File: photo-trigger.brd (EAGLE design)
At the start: 93.4 x 70.3 mm, 49 parts, among them Q1 PN2907, Q2 PN2907, Q3 20MHz, U1 ATMEGA324PA-PU

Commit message: correct device name to match library
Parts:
- VR1, VR2: value RECOMREE-0505S -> RECOM-REE-0505S
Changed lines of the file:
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@@
 <attribute name="VALUE" x="52.07" y="9.525" size="1.27" layer="27"/>
 </element>
-<element name="VR2" library="djm" package="RECOM-REE" value="RECOMREE-0505S" x="39.37" y="59.69"/>
+<element name="VR2" library="djm" package="RECOM-REE" value="RECOM-REE-0505S" x="39.37" y="59.69"/>
 <element name="C3" library="rcl" package="C050-035X075" value="0.1uF" x="49.53" y="63.5" smashed="yes" rot="R180">
 <attribute name="NAME" x="48.006" y="67.056" size="1.27" layer="25" ratio="10" rot="R180"/>
@@
 <attribute name="VALUE" x="6.604" y="20.701" size="1.27" layer="27" ratio="10"/>
 </element>
-<element name="VR1" library="djm" package="RECOM-REE" value="RECOMREE-0505S" x="12.7" y="16.51" smashed="yes" rot="R180">
+<element name="VR1" library="djm" package="RECOM-REE" value="RECOM-REE-0505S" x="12.7" y="16.51" smashed="yes" rot="R180">
 <attribute name="NAME" x="21.59" y="23.495" size="1.27" layer="25" rot="R180"/>
 <attribute name="VALUE" x="22.225" y="14.605" size="1.27" layer="27" rot="R180"/>

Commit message: revised after building v1.0 boards; lots of fixes
ripped out power status indicator circuit - it didn't work.
replaced with a simple power LED.

fixed footprint problem for Recom REE isolated VRMs

rewired LCD socket to be easier to handle at the LCD end

fixed MCU AREF and AGND

expanded prototype area; embiggened pads to make them easier to
solder
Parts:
- removed D1: 6.2V, diode:DO35Z10
- removed Q1, Q2: PN2907, djm:TO92-EBC
- removed R4: 100K, rcl:0207/10
- removed R5: 470, rcl:0207/10
- added +5VI: +5VI, wirepad:1,6/0,9
- added +5VO: +5VO, wirepad:1,6/0,9
- added C8: 0.1uF, rcl:C050-035X075
- added C9: 10uF, rcl:C050-035X075
- added GNDI: GNDI, wirepad:1,6/0,9
- added GNDO: GNDO, wirepad:1,6/0,9
- added GNDP2: GND, wirepad:1,6/0,9
- added VCCP2: VCC, wirepad:1,6/0,9
- LCD: value LCD -> (none)
- R1: value 100K -> 100
- VR1, VR2: value RECOM-REE-0505S -> REE-0505S
- VR3: value RECOM-R-785.0-0.5 -> R-785.0-0.5
- moved R2 75.6 mm to (85.1, 30.5), turned to 90 degrees
- moved C3 40.8 mm to (8.89, 59.7)
- moved C2 31.8 mm to (15.2, 22.9)
- moved VR3 31.8 mm to (8.89, 25.4)
- moved C4 31.7 mm to (15.2, 27.9)
- moved VR2 29.0 mm to (11.4, 52.1), turned to 180 degrees
- moved VR1 26.7 mm to (11.4, 43.2)
- moved R3 19.7 mm to (10.2, 16.5)
- moved R8 17.8 mm to (22.9, 25.4), turned to 270 degrees
- moved C1 15.3 mm to (8.89, 39.4), turned to 180 degrees
- moved R1 13.7 mm to (27.9, 39.4), turned to 270 degrees
- moved R9 4.58 mm to (26.7, 25.4)
- renumbered JP5 to LCD
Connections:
- removed net BATT_LOW: JP8.6, R5.1
- removed net LCD_CONTRAST: LCD.16, TRIM1.P$2
- removed net LCD_DB_4: LCD.7, U1.17
- removed net LCD_DB_5: LCD.9, U1.16
- removed net LCD_DB_6: LCD.11, U1.15
- removed net LCD_DB_7: LCD.13, U1.14
- removed net N$20: D1.A, R1.2, R2.1
- removed net N$21: Q1.B, R2.2
- removed net N$22: Q1.C, R3.2, R4.1
- removed net N$27: Q2.C, R5.2
- removed net N$43: Q2.B, R4.2
- new net AREF: C8.1, U1.32
- new net AVCC: R1.2, U1.30
- new net LCD_DB4: LCD.11, U1.17
- new net LCD_DB5: LCD.12, U1.16
- new net LCD_DB6: LCD.13, U1.15
- new net LCD_DB7: LCD.14, U1.14
- new net LCD_UNU: LCD.10, LCD.7, LCD.8, LCD.9, R2.1
- new net LCD_V0: LCD.3, TRIM1.P$2
- net +5V: now also +5VI.1
- net GND: now also C8.2, C9.2, GNDP2.1, JP8.6, LCD.1, LCD.16, R2.2, TRIM1.P$3; no longer LCD.10, LCD.12, LCD.14, LCD.2, LCD.4, LCD.6, LCD.8, R1.1, TRIM1.P$1, U1.32
- net GNDI: now also GNDO.1
- net GNDIO: now also GNDI.1
- net LCD_EN: now also LCD.6; no longer LCD.1
- net LCD_RS: now also LCD.4; no longer LCD.5
- net LCD_RW: now also LCD.5; no longer LCD.3
- net VCC: now also C9.1, LCD.2, R1.1, R3.2, TRIM1.P$1, VCCP2.1; no longer TRIM1.P$3, U1.30
- net VDD: now also +5VO.1
- net VIN: no longer D1.C, Q1.E, Q2.E
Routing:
- net +5V: track 36.6 -> 96.2 mm
- net VCC: track 230.0 -> 284.9 mm
- net VIN: track 87.5 -> 35.1 mm
- net LCD_DB7: track 0.00 -> 38.7 mm
- net VDD: track 75.3 -> 107.2 mm
- net AVCC: track 0.00 -> 31.5 mm
- net LCD_DB_7: track 30.8 -> 0.00 mm
- net BATT_OK: track 38.2 -> 9.42 mm
- net LCD_DB6: track 0.00 -> 28.2 mm
- net LCD_DB5: track 0.00 -> 27.5 mm
- net BATT_LOW: track 27.2 -> 0.00 mm
- net N$22: track 25.2 -> 0.00 mm, vias 0 -> 1
- net LCD_DB_6: track 24.2 -> 0.00 mm
- net LCD_DB_5: track 22.1 -> 0.00 mm
- net LCD_UNU: track 0.00 -> 20.6 mm
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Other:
- board text added: "+5V O"
- board text added: "DOUT"
- board text added: "GND I"
- board text added: "GND O"
- board text added: "Lighting controller v1.1 2014/08 djm"
- board text added: "VCC"
- board text removed: "DIN"
- board text removed: "GNDI"
- board text removed: "Lighting controller v1.0 2014/07 djm"

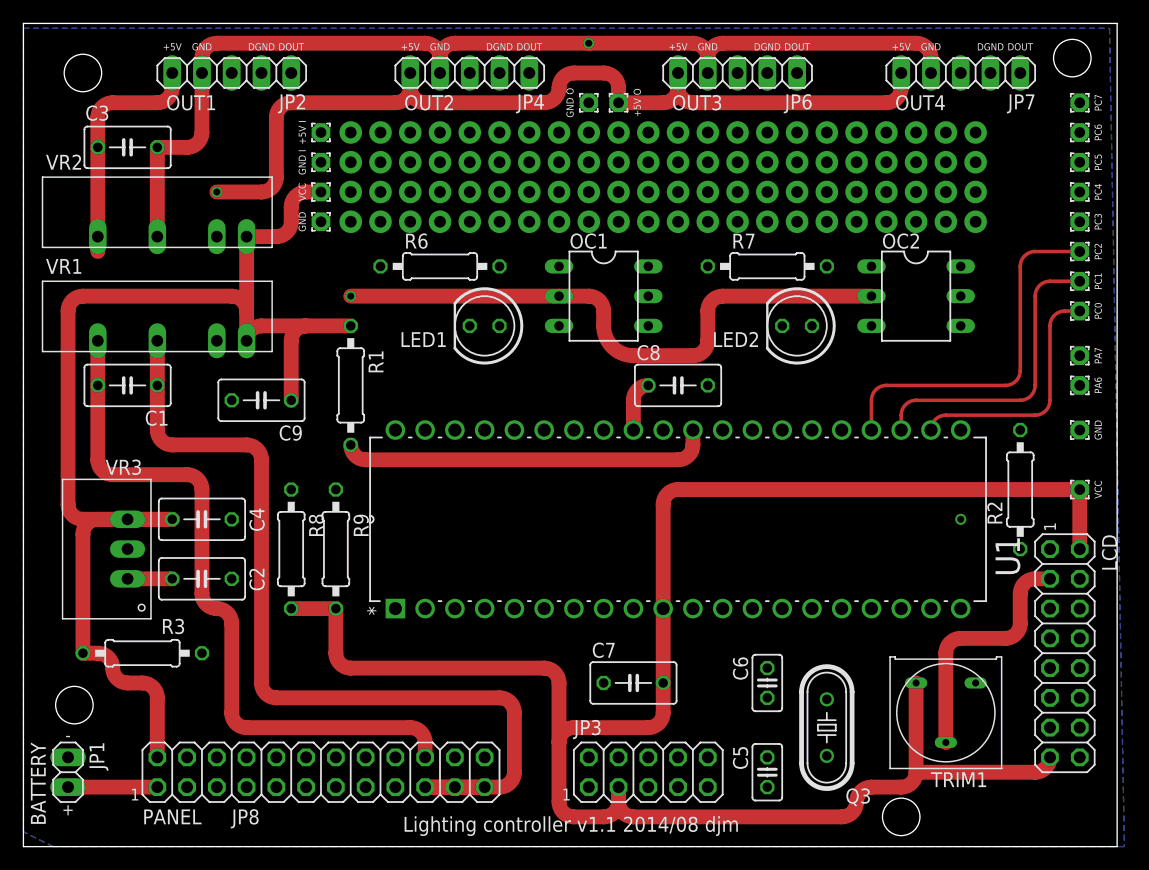
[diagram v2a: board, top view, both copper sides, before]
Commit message: few more layout tweaks; embiggen more wirepads
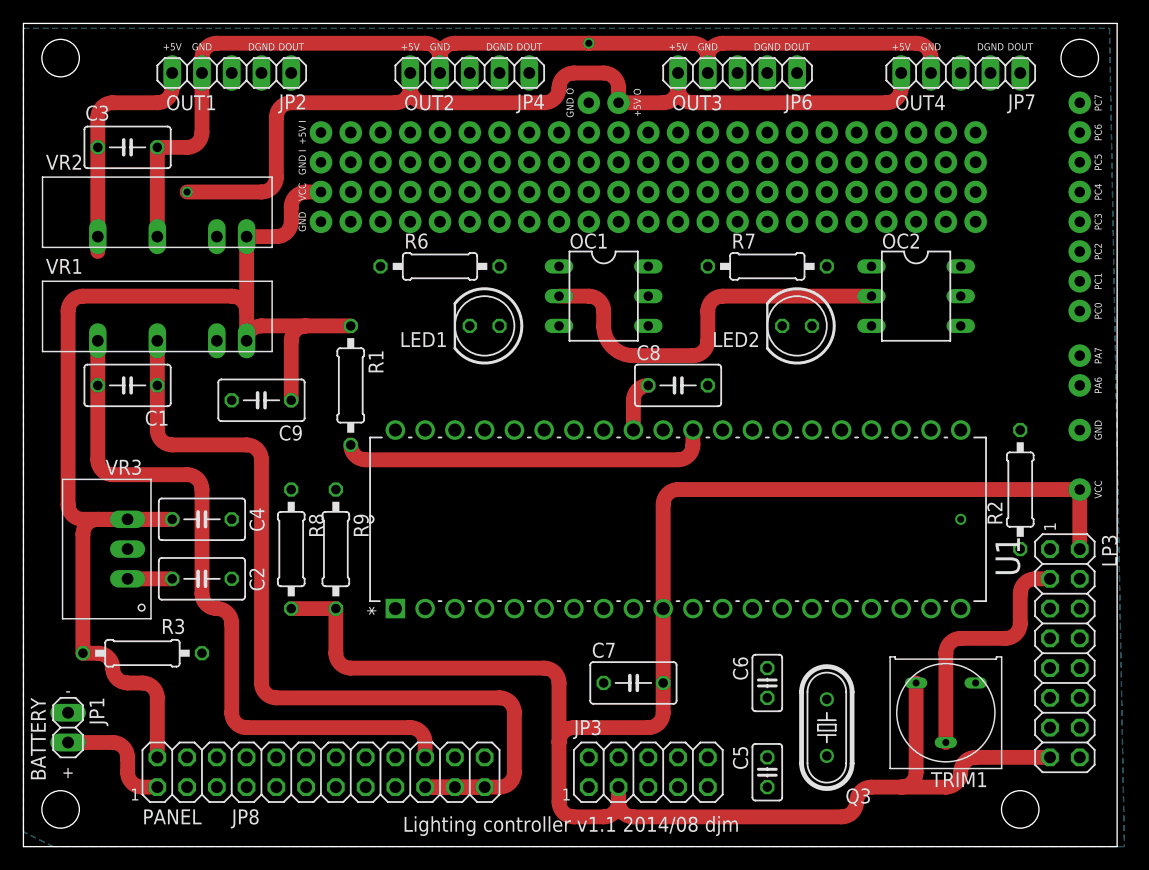
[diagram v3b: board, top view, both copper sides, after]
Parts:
- +5VI, +5VO, GND, GNDI, GNDO, GNDP2, PA6, PA7, PC0, PC1, PC2, PC3, PC4, PC5, PC6, PC7, VCC, VCCP2: device wirepad:1,6/0,9 -> djm:PAD1.9/0.9
- LP3: value (none) -> LCD
- moved JP1 3.81 mm to (3.81, 10.2)
- renumbered LCD to LP3
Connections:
- net +5V: now also +5VI.P$1; no longer +5VI.1
- net GND: now also GND.P$1, GNDP2.P$1; no longer GND.1, GNDP2.1
- net GNDI: now also GNDO.P$1; no longer GNDO.1
- net GNDIO: now also GNDI.P$1; no longer GNDI.1
- net PA6: now also PA6.P$1; no longer PA6.1
- net PA7: now also PA7.P$1; no longer PA7.1
- net PC0: now also PC0.P$1; no longer PC0.1
- net PC1: now also PC1.P$1; no longer PC1.1
- net PC2: now also PC2.P$1; no longer PC2.1
- net PC3: now also PC3.P$1; no longer PC3.1
- net PC4: now also PC4.P$1; no longer PC4.1
- net PC5: now also PC5.P$1; no longer PC5.1
- net PC6: now also PC6.P$1; no longer PC6.1
- net PC7: now also PC7.P$1; no longer PC7.1
- net VCC: now also VCC.P$1, VCCP2.P$1; no longer VCC.1, VCCP2.1
- net VDD: now also +5VO.P$1; no longer +5VO.1
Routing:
- net BATT+: track 7.62 -> 9.94 mm
- net VCC: track 284.9 -> 286.7 mm
- net PC3: track 34.4 -> 35.1 mm
- net PC6: track 49.6 -> 50.4 mm
- net PC5: track 44.5 -> 45.3 mm
- net PC7: track 54.7 -> 55.4 mm
- net PC4: track 39.5 -> 38.7 mm
- net GNDIO: track 161.3 -> 161.8 mm, vias 1 -> 0
